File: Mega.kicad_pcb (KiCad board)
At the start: 2 copper layers, 101.5 x 53.3 mm, 82 parts, among them J1 JTAG, J10 ANALOG-HIGH, J11 Conn_02x18_Odd_Even, J12 DIGITAL-LOW, J2 POWER, J3 EXTRA, J4 ICSP, J5 ANALOG-LOW, J6 DIGITAL-MID, J7 DIGITAL-LOW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

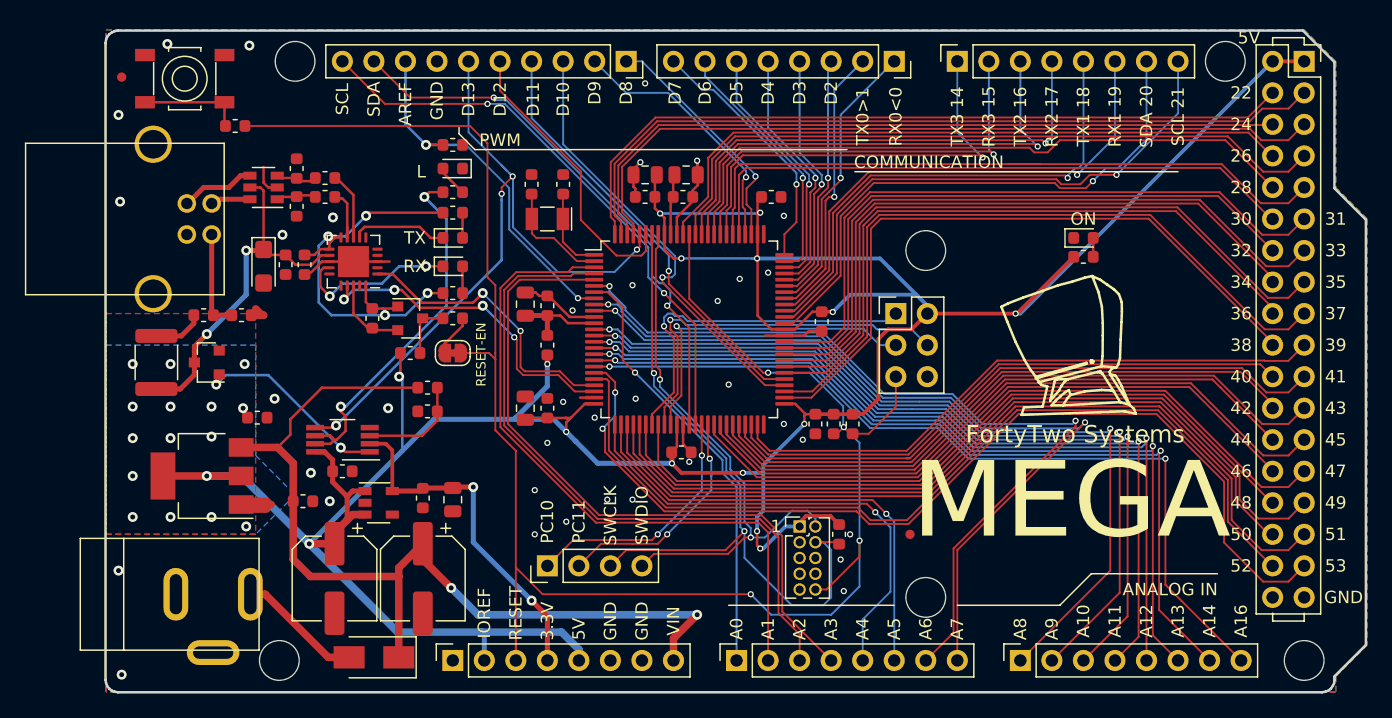
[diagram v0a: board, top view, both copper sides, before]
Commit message: Fix crossed SWD traces and move to KiCAD 5.99
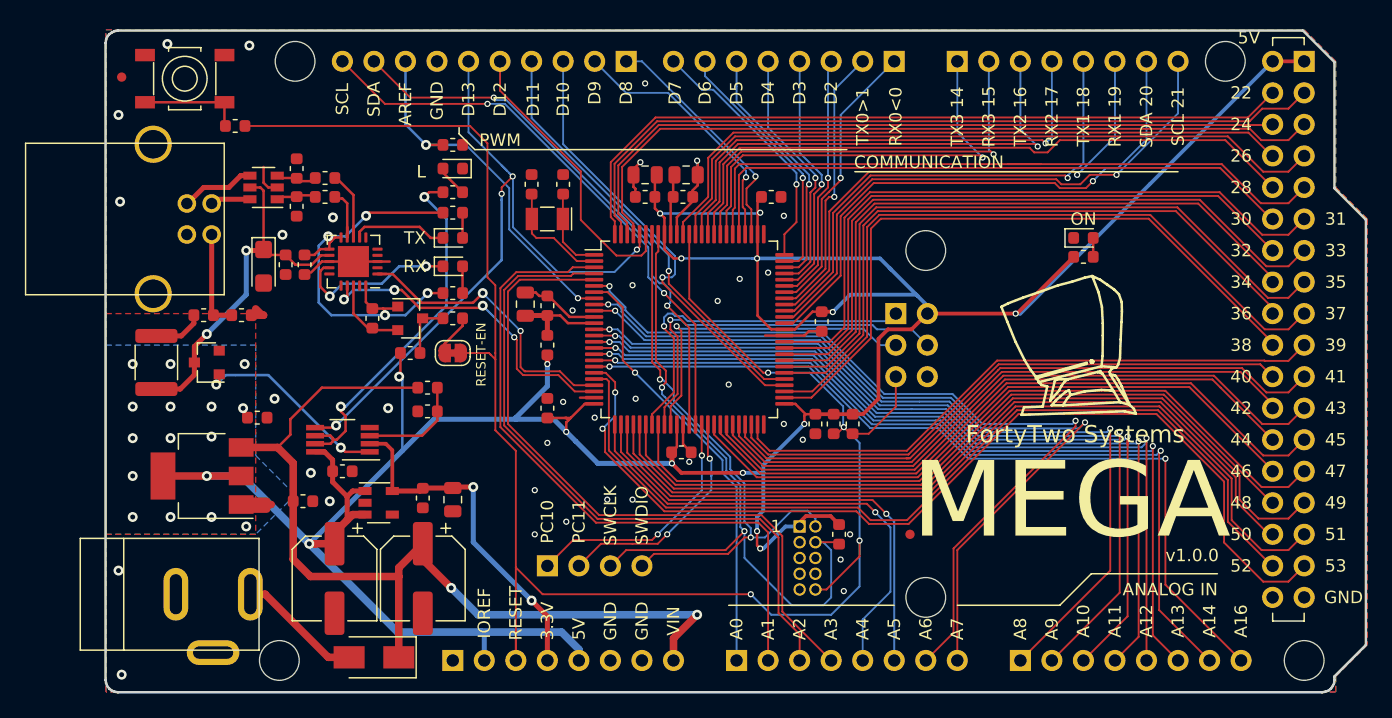
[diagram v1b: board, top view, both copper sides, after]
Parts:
- removed C1: 10uF, Capacitor_SMD:C_0805_2012Metric
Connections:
- U1 pad 93: /SWDIO -> /SWCLK
- U1 pad 94: /SWCLK -> /SWDIO
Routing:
- net +5V: track 276.0 -> 274.1 mm
- net /SWCLK: track 57.3 -> 58.8 mm
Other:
- board text added: "v1.0.0"
